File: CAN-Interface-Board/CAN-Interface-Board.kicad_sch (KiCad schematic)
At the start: 13 parts, among them CN1 Limit Switch Connector 1, CN2 Limit Switch Connector 2, CN3 Encoder Connector, CN5 XY-B3B-XH-A, CN6 MOLEX_26013114, CN7 MOLEX_CAN_IN, CN8 MOLEX_CAN_OUT

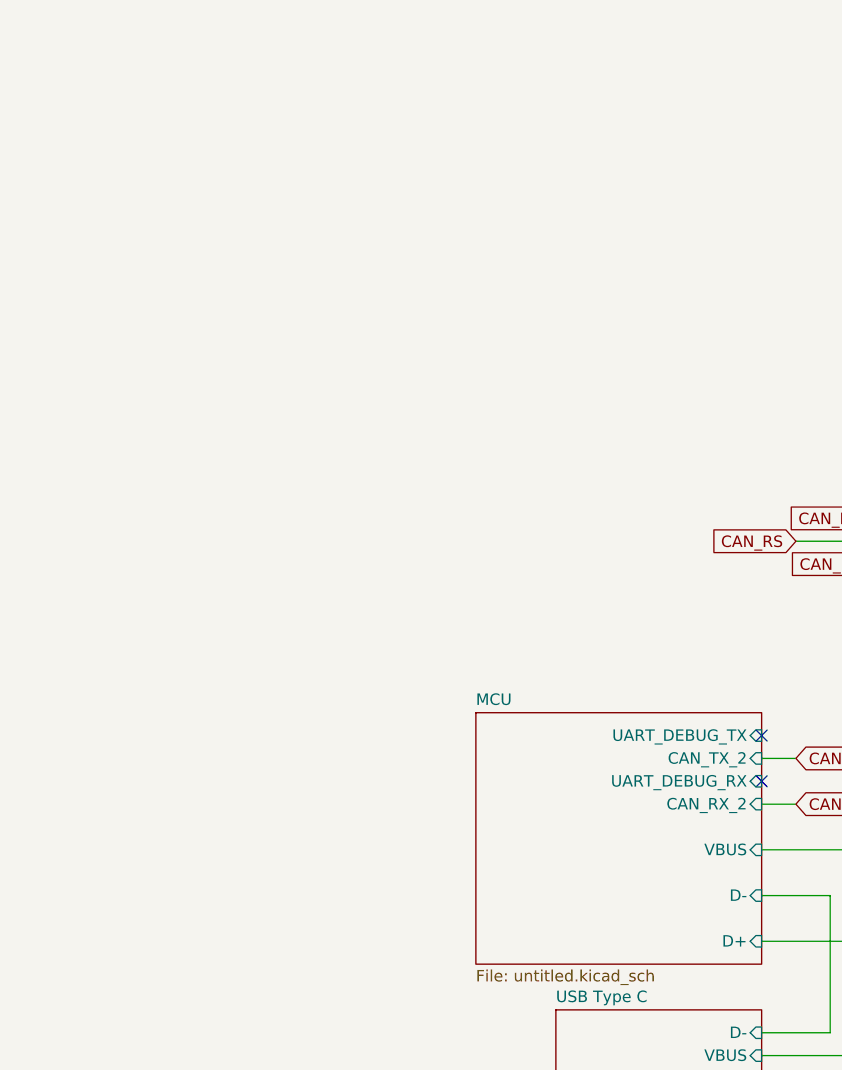
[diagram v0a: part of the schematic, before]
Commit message: Began conversion for full CAS Control
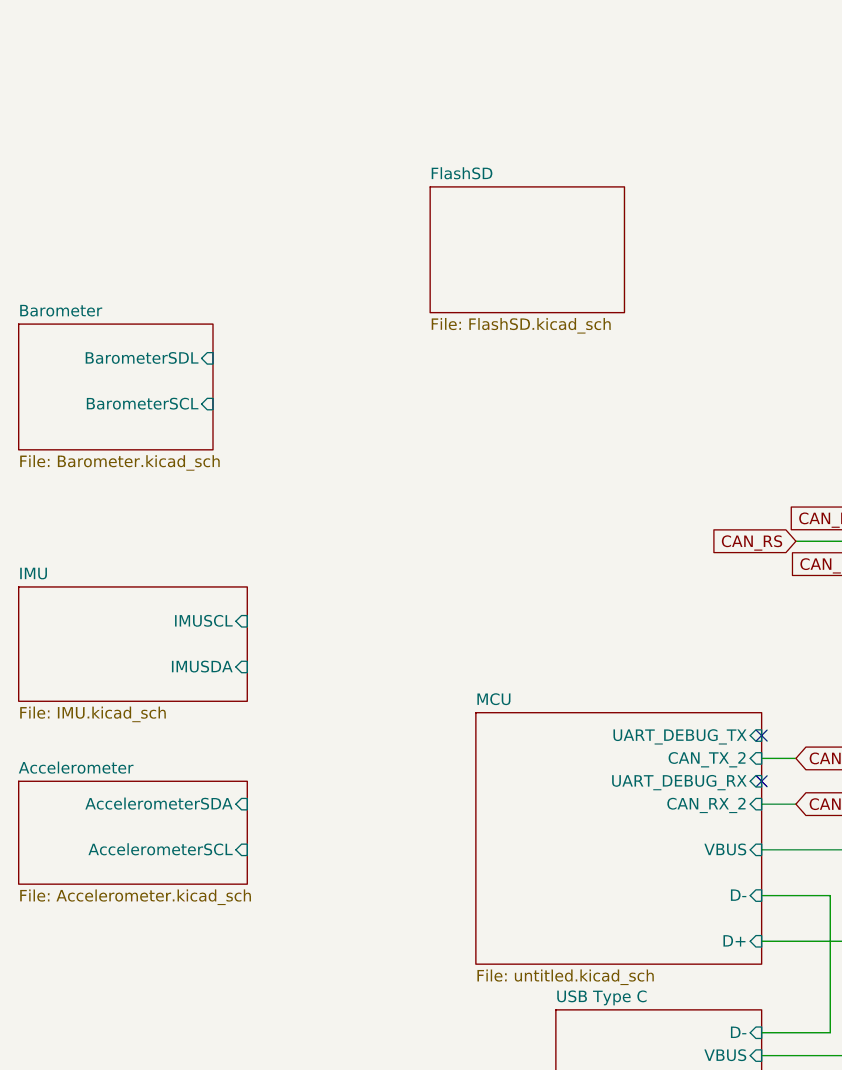
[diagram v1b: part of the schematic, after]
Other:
- added sheet Accelerometer (Accelerometer.kicad_sch)
- added sheet Barometer (Barometer.kicad_sch)
- added sheet FlashSD (FlashSD.kicad_sch)
- added sheet IMU (IMU.kicad_sch)
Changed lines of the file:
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@@
+	)
+	(sheet
+		(at 21.59 90.17)
+		(size 25.4 12.7)
+		(exclude_from_sim no)
+		(in_bom yes)
+		(on_board yes)
+		(dnp no)
+		(fields_autoplaced yes)
+		(stroke
+			(width 0.1524)
+			(type solid)
+		)
+		(fill
+			(color 0 0 0 0.0000)
+		)
+		(property "Sheetname" "IMU"
+			(at 21.59 89.4584 0)
+			(effects
+				(font
+					(size 1.27 1.27)
+				)
+				(justify left bottom)
+			)
+		)
+		(property "Sheetfile" "IMU.kicad_sch"
+			(at 21.59 103.4546 0)
+			(effects
+				(font
+					(size 1.27 1.27)
+				)
+				(justify left top)
+			)
+		)
+		(pin "IMUSCL" input
+			(at 46.99 93.98 0)
+			(effects
+				(font
+					(size 1.27 1.27)
+				)
+				(justify right)
+			)
+		)
+		(pin "IMUSDA" input
+			(at 46.99 99.06 0)
+			(effects
+				(font
+					(size 1.27 1.27)
+				)
+				(justify right)
+			)
+		)
+		(instances
+			(project "CAN-Interface-Board"
+				(path "/8a3e7f99-4046-40e8-bd7c-d9d1c8c7162e"
+					(page "9")
+				)
+			)
+		)
 	)
 	(sheet
@@
 	)
 	(sheet
+		(at 67.31 45.72)
+		(size 21.59 13.97)
+		(exclude_from_sim no)
+		(in_bom yes)
+		(on_board yes)
+		(dnp no)
+		(fields_autoplaced yes)
+		(stroke
+			(width 0.1524)
+			(type solid)
+		)
+		(fill
+			(color 0 0 0 0.0000)
+		)
+		(property "Sheetname" "FlashSD"
+			(at 67.31 45.0084 0)
+			(effects
+				(font
+					(size 1.27 1.27)
+				)
+				(justify left bottom)
+			)
+		)
+		(property "Sheetfile" "FlashSD.kicad_sch"
+			(at 67.31 60.2746 0)
+			(effects
+				(font
+					(size 1.27 1.27)
+				)
+				(justify left top)
+			)
+		)
+		(instances
+			(project "CAN-Interface-Board"
+				(path "/8a3e7f99-4046-40e8-bd7c-d9d1c8c7162e"
+					(page "7")
+				)
+			)
+		)
+	)
+	(sheet
+		(at 21.59 60.96)
+		(size 21.59 13.97)
+		(exclude_from_sim no)
+		(in_bom yes)
+		(on_board yes)
+		(dnp no)
+		(fields_autoplaced yes)
+		(stroke
+			(width 0.1524)
+			(type solid)
+		)
+		(fill
+			(color 0 0 0 0.0000)
+		)
+		(property "Sheetname" "Barometer"
+			(at 21.59 60.2484 0)
+			(effects
+				(font
+					(size 1.27 1.27)
+				)
+				(justify left bottom)
+			)
+		)
+		(property "Sheetfile" "Barometer.kicad_sch"
+			(at 21.59 75.5146 0)
+			(effects
+				(font
+					(size 1.27 1.27)
+				)
+				(justify left top)
+			)
+		)
+		(pin "BarometerSDL" input
+			(at 43.18 64.77 0)
+			(effects
+				(font
+					(size 1.27 1.27)
+				)
+				(justify right)
+			)
+		)
+		(pin "BarometerSCL" input
+			(at 43.18 69.85 0)
+			(effects
+				(font
+					(size 1.27 1.27)
+				)
+				(justify right)
+			)
+		)
+		(instances
+			(project "CAN-Interface-Board"
+				(path "/8a3e7f99-4046-40e8-bd7c-d9d1c8c7162e"
+					(page "8")
+				)
+			)
+		)
+	)
+	(sheet
 		(at 72.39 104.14)
 		(size 31.75 27.94)
@@
 				)
 			)
+		)
+	)
+	(sheet
+		(at 21.59 111.76)
+		(size 25.4 11.43)
+		(exclude_from_sim no)
+		(in_bom yes)
+		(on_board yes)
+		(dnp no)
+		(fields_autoplaced yes)
+		(stroke
+			(width 0.1524)
+			(type solid)
+		)
+		(fill
+			(color 0 0 0 0.0000)
+		)
+		(property "Sheetname" "Accelerometer"
+			(at 21.59 111.0484 0)
+			(effects
+				(font
+					(size 1.27 1.27)
+				)
+				(justify left bottom)
+			)
+		)
+		(property "Sheetfile" "Accelerometer.kicad_sch"
+			(at 21.59 123.7746 0)
+			(effects
+				(font
+					(size 1.27 1.27)
+				)
+				(justify left top)
+			)
+		)
+		(pin "AccelerometerSDA" input
+			(at 46.99 114.3 0)
+			(effects
+				(font
+					(size 1.27 1.27)
+				)
+				(justify right)
+			)
+		)
+		(pin "AccelerometerSCL" input
+			(at 46.99 119.38 0)
+			(effects
+				(font
+					(size 1.27 1.27)
+				)
+				(justify right)
+			)
+		)
+		(instances
+			(project "CAN-Interface-Board"
+				(path "/8a3e7f99-4046-40e8-bd7c-d9d1c8c7162e"
+					(page "10")
+				)
+			)

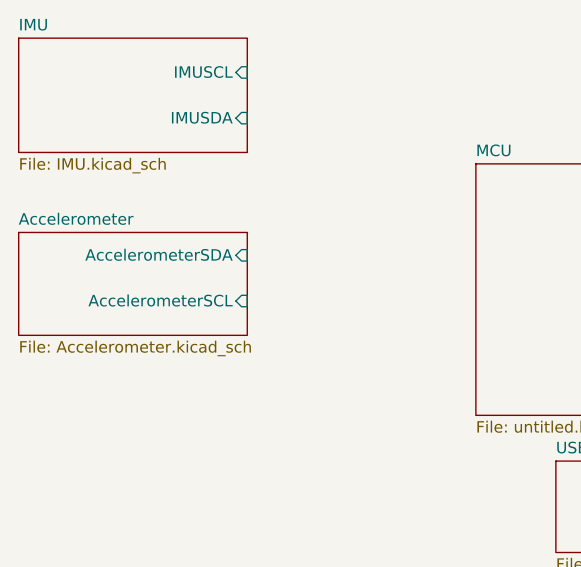
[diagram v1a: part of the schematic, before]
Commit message: altered sensor schematics
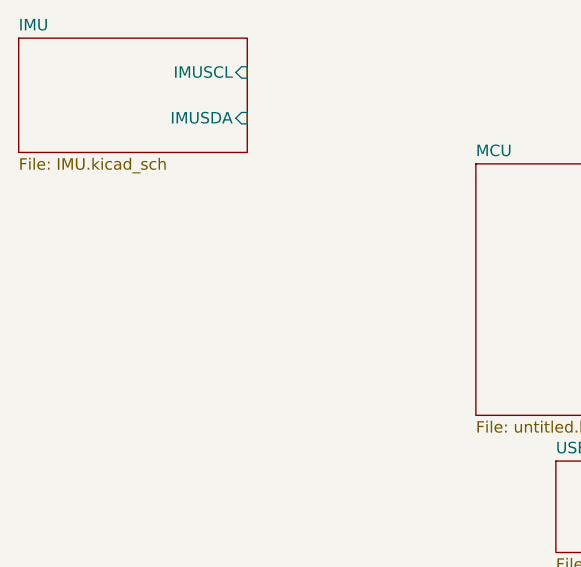
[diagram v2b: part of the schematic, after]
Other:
- removed sheet Accelerometer
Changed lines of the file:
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@@
-	)
-	(sheet
-		(at 21.59 111.76)
-		(size 25.4 11.43)
-		(exclude_from_sim no)
-		(in_bom yes)
-		(on_board yes)
-		(dnp no)
-		(fields_autoplaced yes)
-		(stroke
-			(width 0.1524)
-			(type solid)
-		)
-		(fill
-			(color 0 0 0 0.0000)
-		)
-		(property "Sheetname" "Accelerometer"
-			(at 21.59 111.0484 0)
-			(effects
-				(font
-					(size 1.27 1.27)
-				)
-				(justify left bottom)
-			)
-		)
-		(property "Sheetfile" "Accelerometer.kicad_sch"
-			(at 21.59 123.7746 0)
-			(effects
-				(font
-					(size 1.27 1.27)
-				)
-				(justify left top)
-			)
-		)
-		(pin "AccelerometerSDA" input
-			(at 46.99 114.3 0)
-			(effects
-				(font
-					(size 1.27 1.27)
-				)
-				(justify right)
-			)
-		)
-		(pin "AccelerometerSCL" input
-			(at 46.99 119.38 0)
-			(effects
-				(font
-					(size 1.27 1.27)
-				)
-				(justify right)
-			)
-		)
-		(instances
-			(project "CAN-Interface-Board"
-				(path "/8a3e7f99-4046-40e8-bd7c-d9d1c8c7162e"
-					(page "10")
-				)
-			)
-		)
 	)
 	(sheet

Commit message: editing schematic
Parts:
- removed CN1: Limit Switch Connector 1, custom footprints:JST B2B-XH-A(LF)(SN), symbol custom symbols:JST B2B-XH-A(LF)(SN)
- removed CN2: Limit Switch Connector 2, custom footprints:JST B2B-XH-A(LF)(SN), symbol custom symbols:JST B2B-XH-A(LF)(SN)
- removed CN5: XY-B3B-XH-A, custom footprints:CONN-TH_3P-P2.50_A2501WV2-3P, symbol custom symbols:XY-B3B-XH-A
- removed CN6: MOLEX_26013114, custom footprints:MOLEX 26013114, symbol custom symbols:MOLEX_26013114
- removed CN7: MOLEX_CAN_IN, custom footprints:MOLEX 26013114, symbol custom symbols:MOLEX_26013114
- removed CN8: MOLEX_CAN_OUT, custom footprints:MOLEX 26013114, symbol custom symbols:MOLEX_26013114
- removed J_BUCK_IN_A1, J_BUCK_IN_B1, J_BUCK_OUT_A1, J_BUCK_OUT_B1: ~, Connector_PinSocket_2.54mm:PinSocket_1x02_P2.54mm_Horizontal, symbol Connector_Generic:Conn_01x02
- removed R2, R3: 10K, Resistor_SMD:R_0805_2012Metric_Pad1.20x1.40mm_HandSolder, symbol Device:R
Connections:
- no-connect marks 3 -> 1
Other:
- sheet LDO_3.3v renamed Power
- added sheet Servo (Servo.kicad_sch)
- sheet CAN Transciever ports: added CAN_RX_2, CAN_TX_2; removed CANH, CANL, D, R, RS
- sheet Current Sensor ports: added BuckOut, VoltageADC; removed Signal, V-buck-in, V-buck-out
- sheet FlashSD ports: added SDCLK, SDMISO, SDMOSI; removed none
- sheet MCU: file untitled.kicad_sch -> MCU.kicad_sch
- sheet Power: file LD0_3n3v.kicad_sch -> Power.kicad_sch
- moved on the sheet: CN3
